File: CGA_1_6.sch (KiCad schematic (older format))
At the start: 19 parts, among them U13 74LS08, U14 74LS32, U28 74LS10, U38 MC6845, U48 74LS51, U49 74LS02, U50 2118, U51 2118, U52 2118, U53 2118, U54 2118, U55 2118, U56 2118, U57 2118, U58 74LS374, U59 74LS374, U60 74LS374, U61 74LS374, U62 74LS125

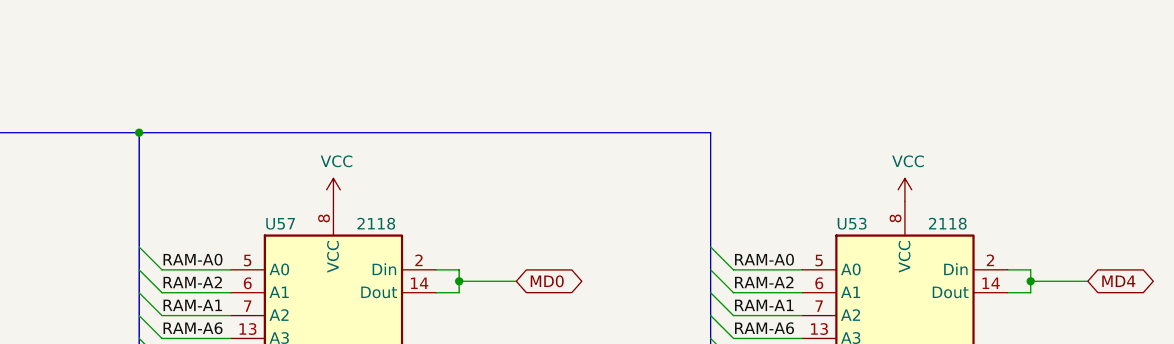
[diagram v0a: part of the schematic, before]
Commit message: Added note on RAM chips
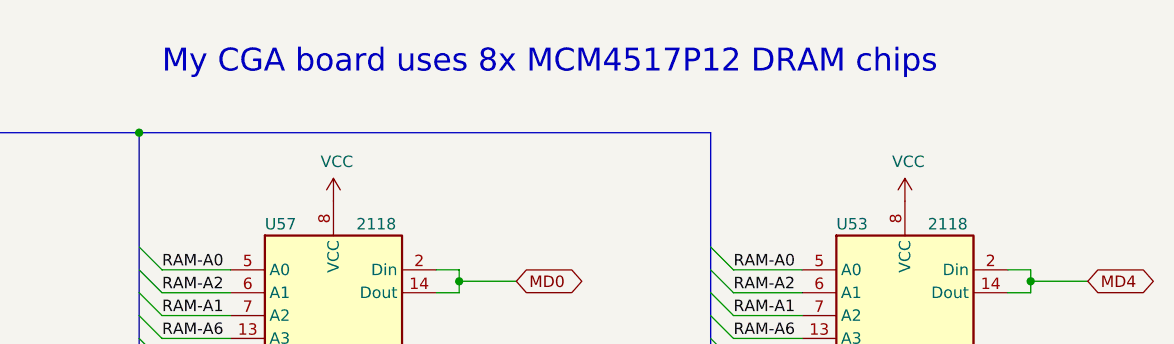
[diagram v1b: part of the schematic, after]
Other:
- note added: "My CGA board uses 8x MCM4517P12 DRAM chips"
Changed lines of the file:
@@
 Wire Bus Line
 	13850 1200 13850 8550
+Text Notes 11450 950  0    100  ~ 0
+My CGA board uses 8x MCM4517P12 DRAM chips
 $EndSCHEMATC

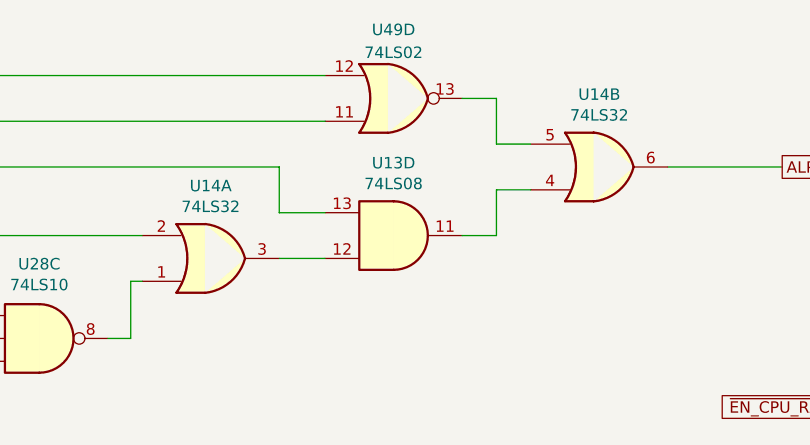
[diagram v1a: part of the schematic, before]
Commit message: Reorganize space between ICs
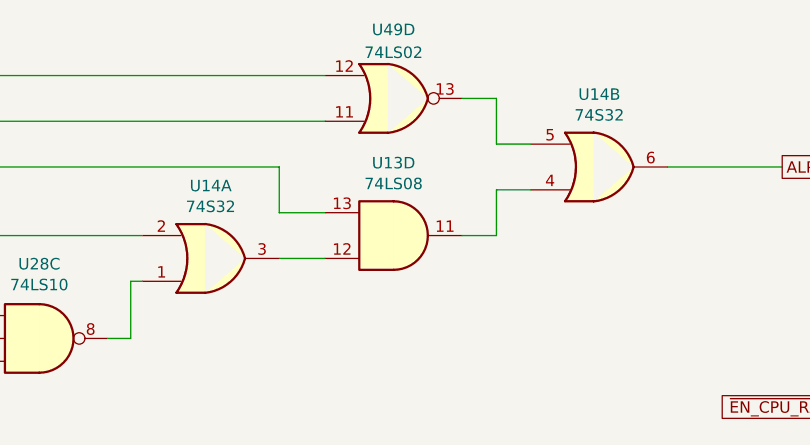
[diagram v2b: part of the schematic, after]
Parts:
- U14: value 74LS32 -> 74S32
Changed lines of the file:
@@
 P 5250 1350
 F 0 "U14" H 5250 1033 50  0000 C CNN
-F 1 "74LS32" H 5250 1124 50  0000 C CNN
+F 1 "74S32" H 5250 1124 50  0000 C CNN
 F 2 "Package_DIP:DIP-14_W7.62mm_LongPads" H 5250 1350 50  0001 C CNN
 F 3 "http://www.ti.com/lit/gpn/sn74LS32" H 5250 1350 50  0001 C CNN
@@
 P 3550 1750
 F 0 "U14" H 3550 1433 50  0000 C CNN
-F 1 "74LS32" H 3550 1524 50  0000 C CNN
+F 1 "74S32" H 3550 1524 50  0000 C CNN
 F 2 "Package_DIP:DIP-14_W7.62mm_LongPads" H 3550 1750 50  0001 C CNN
 F 3 "http://www.ti.com/lit/gpn/sn74LS32" H 3550 1750 50  0001 C CNN

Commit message: Changed footprints, moving components
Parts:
- U13, U14, U28, U48, U62: footprint Package_DIP:DIP-14_W7.62mm_LongPads -> Package_DIP:DIP-14_W7.62mm
- U38: footprint Package_DIP:DIP-40_W15.24mm_LongPads -> Package_DIP:DIP-40_W15.24mm
- U49: footprint (none) -> Package_DIP:DIP-14_W7.62mm
- U50, U51, U52, U53, U54, U55, U56, U57: footprint Package_DIP:DIP-16_W7.62mm_LongPads -> Package_DIP:DIP-16_W7.62mm
- U58, U59, U60, U61: footprint Package_DIP:DIP-20_W7.62mm_LongPads -> Package_DIP:DIP-20_W7.62mm
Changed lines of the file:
@@
 F 0 "U57" H 11900 3800 50  0000 L CNN
 F 1 "2118" H 12300 3800 50  0000 L CNN
-F 2 "Package_DIP:DIP-16_W7.62mm_LongPads" H 12350 2650 50  0001 C CNN
+F 2 "Package_DIP:DIP-16_W7.62mm" H 12350 2650 50  0001 C CNN
 F 3 "" H 12350 2700 50  0001 C CNN
 	1    12350 2700
@@
 F 0 "U56" H 11900 5850 50  0000 L CNN
 F 1 "2118" H 12300 5850 50  0000 L CNN
-F 2 "Package_DIP:DIP-16_W7.62mm_LongPads" H 12350 4700 50  0001 C CNN
+F 2 "Package_DIP:DIP-16_W7.62mm" H 12350 4700 50  0001 C CNN
 F 3 "" H 12350 4750 50  0001 C CNN
 	1    12350 4750
@@
 F 0 "U55" H 11900 7900 50  0000 L CNN
 F 1 "2118" H 12300 7900 50  0000 L CNN
-F 2 "Package_DIP:DIP-16_W7.62mm_LongPads" H 12350 6750 50  0001 C CNN
+F 2 "Package_DIP:DIP-16_W7.62mm" H 12350 6750 50  0001 C CNN
 F 3 "" H 12350 6800 50  0001 C CNN
 	1    12350 6800
@@
 F 0 "U54" H 11900 10050 50  0000 L CNN
 F 1 "2118" H 12300 10050 50  0000 L CNN
-F 2 "Package_DIP:DIP-16_W7.62mm_LongPads" H 12350 8900 50  0001 C CNN
+F 2 "Package_DIP:DIP-16_W7.62mm" H 12350 8900 50  0001 C CNN
 F 3 "" H 12350 8950 50  0001 C CNN
 	1    12350 8950
@@
 F 0 "U53" H 14400 3800 50  0000 L CNN
 F 1 "2118" H 14800 3800 50  0000 L CNN
-F 2 "Package_DIP:DIP-16_W7.62mm_LongPads" H 14850 2650 50  0001 C CNN
+F 2 "Package_DIP:DIP-16_W7.62mm" H 14850 2650 50  0001 C CNN
 F 3 "" H 14850 2700 50  0001 C CNN
 	1    14850 2700
@@
 F 0 "U52" H 14400 5850 50  0000 L CNN
 F 1 "2118" H 14800 5850 50  0000 L CNN
-F 2 "Package_DIP:DIP-16_W7.62mm_LongPads" H 14850 4700 50  0001 C CNN
+F 2 "Package_DIP:DIP-16_W7.62mm" H 14850 4700 50  0001 C CNN
 F 3 "" H 14850 4750 50  0001 C CNN
 	1    14850 4750
@@
 F 0 "U51" H 14400 7900 50  0000 L CNN
 F 1 "2118" H 14800 7900 50  0000 L CNN
-F 2 "Package_DIP:DIP-16_W7.62mm_LongPads" H 14850 6750 50  0001 C CNN
+F 2 "Package_DIP:DIP-16_W7.62mm" H 14850 6750 50  0001 C CNN
 F 3 "" H 14850 6800 50  0001 C CNN
 	1    14850 6800
@@
 F 0 "U50" H 14400 10050 50  0000 L CNN
 F 1 "2118" H 14800 10050 50  0000 L CNN
-F 2 "Package_DIP:DIP-16_W7.62mm_LongPads" H 14850 8900 50  0001 C CNN
+F 2 "Package_DIP:DIP-16_W7.62mm" H 14850 8900 50  0001 C CNN
 F 3 "" H 14850 8950 50  0001 C CNN
 	1    14850 8950
@@
 F 0 "U60" H 8400 2550 50  0000 C CNN
 F 1 "74LS374" H 8850 2550 50  0000 C CNN
-F 2 "Package_DIP:DIP-20_W7.62mm_LongPads" H 8650 1900 50  0001 C CNN
+F 2 "Package_DIP:DIP-20_W7.62mm" H 8650 1900 50  0001 C CNN
 F 3 "http://www.ti.com/lit/gpn/sn74LS374" H 8650 1900 50  0001 C CNN
 	1    8650 1900
@@
 F 0 "U61" H 8400 4650 50  0000 C CNN
 F 1 "74LS374" H 8850 4650 50  0000 C CNN
-F 2 "Package_DIP:DIP-20_W7.62mm_LongPads" H 8650 4000 50  0001 C CNN
+F 2 "Package_DIP:DIP-20_W7.62mm" H 8650 4000 50  0001 C CNN
 F 3 "http://www.ti.com/lit/gpn/sn74LS374" H 8650 4000 50  0001 C CNN
 	1    8650 4000
@@
 F 0 "U59" H 8400 6750 50  0000 C CNN
 F 1 "74LS374" H 8850 6750 50  0000 C CNN
-F 2 "Package_DIP:DIP-20_W7.62mm_LongPads" H 8650 6100 50  0001 C CNN
+F 2 "Package_DIP:DIP-20_W7.62mm" H 8650 6100 50  0001 C CNN
 F 3 "http://www.ti.com/lit/gpn/sn74LS374" H 8650 6100 50  0001 C CNN
 	1    8650 6100
@@
 F 0 "U58" H 8400 8850 50  0000 C CNN
 F 1 "74LS374" H 8850 8850 50  0000 C CNN
-F 2 "Package_DIP:DIP-20_W7.62mm_LongPads" H 8650 8200 50  0001 C CNN
+F 2 "Package_DIP:DIP-20_W7.62mm" H 8650 8200 50  0001 C CNN
 F 3 "http://www.ti.com/lit/gpn/sn74LS374" H 8650 8200 50  0001 C CNN
 	1    8650 8200
@@
 F 0 "U62" H 8000 9917 50  0000 C CNN
 F 1 "74LS125" H 8000 9826 50  0000 C CNN
-F 2 "Package_DIP:DIP-14_W7.62mm_LongPads" H 8000 9600 50  0001 C CNN
+F 2 "Package_DIP:DIP-14_W7.62mm" H 8000 9600 50  0001 C CNN
 F 3 "http://www.ti.com/lit/gpn/sn74LS125" H 8000 9600 50  0001 C CNN
 	1    8000 9600
@@
 F 0 "U49" H 6900 10875 50  0000 C CNN
 F 1 "74LS02" H 6900 10784 50  0000 C CNN
-F 2 "" H 6900 10550 50  0001 C CNN
+F 2 "Package_DIP:DIP-14_W7.62mm" H 6900 10550 50  0001 C CNN
 F 3 "http://www.ti.com/lit/gpn/sn74ls02" H 6900 10550 50  0001 C CNN
 	3    6900 10550
@@
 F 0 "U48" H 5950 11075 50  0000 C CNN
 F 1 "74LS51" H 5950 10984 50  0000 C CNN
-F 2 "Package_DIP:DIP-14_W7.62mm_LongPads" H 5950 10550 50  0001 C CNN
+F 2 "Package_DIP:DIP-14_W7.62mm" H 5950 10550 50  0001 C CNN
 F 3 "http://www.ti.com/lit/ds/symlink/sn74ls51.pdf" H 5950 10550 50  0001 C CNN
 	1    5950 10550
@@
 F 0 "U38" H 2850 8550 50  0000 C CNN
 F 1 "MC6845" H 3650 8550 50  0000 C CNN
-F 2 "Package_DIP:DIP-40_W15.24mm_LongPads" H 3350 5850 50  0001 L CNN
+F 2 "Package_DIP:DIP-40_W15.24mm" H 3350 5850 50  0001 L CNN
 F 3 "http://pdf.datasheetcatalog.com/datasheet_pdf/motorola/MC6845L_and_MC6845P.pdf" H 3300 7200 50  0001 C CNN
 	1    3300 7200
@@
 F 0 "U49" H 4350 750 50  0000 C CNN
 F 1 "74LS02" H 4350 850 50  0000 C CNN
-F 2 "" H 4350 1050 50  0001 C CNN
+F 2 "Package_DIP:DIP-14_W7.62mm" H 4350 1050 50  0001 C CNN
 F 3 "http://www.ti.com/lit/gpn/sn74ls02" H 4350 1050 50  0001 C CNN
 	4    4350 1050
@@
 F 0 "U14" H 5250 1033 50  0000 C CNN
 F 1 "74S32" H 5250 1124 50  0000 C CNN
-F 2 "Package_DIP:DIP-14_W7.62mm_LongPads" H 5250 1350 50  0001 C CNN
+F 2 "Package_DIP:DIP-14_W7.62mm" H 5250 1350 50  0001 C CNN
 F 3 "http://www.ti.com/lit/gpn/sn74LS32" H 5250 1350 50  0001 C CNN
 	2    5250 1350
@@
 F 0 "U13" H 4350 1333 50  0000 C CNN
 F 1 "74LS08" H 4350 1424 50  0000 C CNN
-F 2 "Package_DIP:DIP-14_W7.62mm_LongPads" H 4350 1650 50  0001 C CNN
+F 2 "Package_DIP:DIP-14_W7.62mm" H 4350 1650 50  0001 C CNN
 F 3 "http://www.ti.com/lit/gpn/sn74LS08" H 4350 1650 50  0001 C CNN
 	4    4350 1650
@@
 F 0 "U14" H 3550 1433 50  0000 C CNN
 F 1 "74S32" H 3550 1524 50  0000 C CNN
-F 2 "Package_DIP:DIP-14_W7.62mm_LongPads" H 3550 1750 50  0001 C CNN
+F 2 "Package_DIP:DIP-14_W7.62mm" H 3550 1750 50  0001 C CNN
 F 3 "http://www.ti.com/lit/gpn/sn74LS32" H 3550 1750 50  0001 C CNN
 	1    3550 1750
@@
 F 0 "U28" H 2800 2425 50  0000 C CNN
 F 1 "74LS10" H 2800 2334 50  0000 C CNN
-F 2 "Package_DIP:DIP-14_W7.62mm_LongPads" H 2800 2100 50  0001 C CNN
+F 2 "Package_DIP:DIP-14_W7.62mm" H 2800 2100 50  0001 C CNN
 F 3 "http://www.ti.com/lit/gpn/sn74LS10" H 2800 2100 50  0001 C CNN
 	3    2800 2100
@@
 Wire Wire Line
 	11450 6200 11750 6200
+Text Notes 11450 950  0    100  ~ 0
+My CGA board uses 8x MCM4517P12 DRAM chips
 Wire Bus Line
 	9650 1200 9650 8550
@@
 Wire Bus Line
 	13850 1200 13850 8550
-Text Notes 11450 950  0    100  ~ 0
-My CGA board uses 8x MCM4517P12 DRAM chips
 $EndSCHEMATC

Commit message: connect the two NC in DRAM to GND, so ideally 4164 and 41256 can be used
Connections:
- net GND: now also U50.1 (NC), U50.9 (NC), U51.1 (NC), U51.9 (NC), U52.1 (NC), U52.9 (NC), U53.1 (NC), U53.9 (NC), U54.1 (NC), U54.9 (NC), U55.1 (NC), U55.9 (NC), U56.1 (NC), U56.9 (NC), U57.1 (NC), U57.9 (NC)
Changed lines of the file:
@@
 Text Notes 11450 950  0    100  ~ 0
 My CGA board uses 8x MCM4517P12 DRAM chips
+Wire Wire Line
+	12650 2300 12750 2300
+Wire Wire Line
+	12750 2300 12750 2350
+Wire Wire Line
+	12750 2400 12650 2400
+$Comp
+L power:GND #PWR?
+U 1 1 6084F132
+P 12850 2500
+F 0 "#PWR?" H 12850 2250 50  0001 C CNN
+F 1 "GND" H 12855 2327 50  0000 C CNN
+F 2 "" H 12850 2500 50  0001 C CNN
+F 3 "" H 12850 2500 50  0001 C CNN
+	1    12850 2500
+	1    0    0    -1
+$EndComp
+Wire Wire Line
+	12750 2350 12850 2350
+Wire Wire Line
+	12850 2350 12850 2500
+Connection ~ 12750 2350
+Wire Wire Line
+	12750 2350 12750 2400
+Wire Wire Line
+	15150 2300 15250 2300
+Wire Wire Line
+	15250 2300 15250 2350
+Wire Wire Line
+	15250 2400 15150 2400
+$Comp
+L power:GND #PWR?
+U 1 1 6087581A
+P 15350 2500
+F 0 "#PWR?" H 15350 2250 50  0001 C CNN
+F 1 "GND" H 15355 2327 50  0000 C CNN
+F 2 "" H 15350 2500 50  0001 C CNN
+F 3 "" H 15350 2500 50  0001 C CNN
+	1    15350 2500
+	1    0    0    -1
+$EndComp
+Wire Wire Line
+	15250 2350 15350 2350
+Wire Wire Line
+	15350 2350 15350 2500
+Connection ~ 15250 2350
+Wire Wire Line
+	15250 2350 15250 2400
+Wire Wire Line
+	12650 4350 12750 4350
+Wire Wire Line
+	12750 4350 12750 4400
+Wire Wire Line
+	12750 4450 12650 4450
+$Comp
+L power:GND #PWR?
+U 1 1 6089A5C0
+P 12850 4550
+F 0 "#PWR?" H 12850 4300 50  0001 C CNN
+F 1 "GND" H 12855 4377 50  0000 C CNN
+F 2 "" H 12850 4550 50  0001 C CNN
+F 3 "" H 12850 4550 50  0001 C CNN
+	1    12850 4550
+	1    0    0    -1
+$EndComp
+Wire Wire Line
+	12750 4400 12850 4400
+Wire Wire Line
+	12850 4400 12850 4550
+Connection ~ 12750 4400
+Wire Wire Line
+	12750 4400 12750 4450
+Wire Wire Line
+	15150 4350 15250 4350
+Wire Wire Line
+	15250 4350 15250 4400
+Wire Wire Line
+	15250 4450 15150 4450
+$Comp
+L power:GND #PWR?
+U 1 1 608BFDC6
+P 15350 4550
+F 0 "#PWR?" H 15350 4300 50  0001 C CNN
+F 1 "GND" H 15355 4377 50  0000 C CNN
+F 2 "" H 15350 4550 50  0001 C CNN
+F 3 "" H 15350 4550 50  0001 C CNN
+	1    15350 4550
+	1    0    0    -1
+$EndComp
+Wire Wire Line
+	15250 4400 15350 4400
+Wire Wire Line
+	15350 4400 15350 4550
+Connection ~ 15250 4400
+Wire Wire Line
+	15250 4400 15250 4450
+Wire Wire Line
+	12650 6400 12750 6400
+Wire Wire Line
+	12750 6400 12750 6450
+Wire Wire Line
+	12750 6500 12650 6500
+$Comp
+L power:GND #PWR?
+U 1 1 608E60A7
+P 12850 6600
+F 0 "#PWR?" H 12850 6350 50  0001 C CNN
+F 1 "GND" H 12855 6427 50  0000 C CNN
+F 2 "" H 12850 6600 50  0001 C CNN
+F 3 "" H 12850 6600 50  0001 C CNN
+	1    12850 6600
+	1    0    0    -1
+$EndComp
+Wire Wire Line
+	12750 6450 12850 6450
+Wire Wire Line
+	12850 6450 12850 6600
+Connection ~ 12750 6450
+Wire Wire Line
+	12750 6450 12750 6500
+Wire Wire Line
+	15150 6400 15250 6400
+Wire Wire Line
+	15250 6400 15250 6450
+Wire Wire Line
+	15250 6500 15150 6500
+$Comp
+L power:GND #PWR?
+U 1 1 6090D358
+P 15350 6600
+F 0 "#PWR?" H 15350 6350 50  0001 C CNN
+F 1 "GND" H 15355 6427 50  0000 C CNN
+F 2 "" H 15350 6600 50  0001 C CNN
+F 3 "" H 15350 6600 50  0001 C CNN
+	1    15350 6600
+	1    0    0    -1
+$EndComp
+Wire Wire Line
+	15250 6450 15350 6450
+Wire Wire Line
+	15350 6450 15350 6600
+Connection ~ 15250 6450
+Wire Wire Line
+	15250 6450 15250 6500
+Wire Wire Line
+	12650 8550 12750 8550
+Wire Wire Line
+	12750 8550 12750 8600
+Wire Wire Line
+	12750 8650 12650 8650
+$Comp
+L power:GND #PWR?
+U 1 1 6093520C
+P 12850 8750
+F 0 "#PWR?" H 12850 8500 50  0001 C CNN
+F 1 "GND" H 12855 8577 50  0000 C CNN
+F 2 "" H 12850 8750 50  0001 C CNN
+F 3 "" H 12850 8750 50  0001 C CNN
+	1    12850 8750
+	1    0    0    -1
+$EndComp
+Wire Wire Line
+	12750 8600 12850 8600
+Wire Wire Line
+	12850 8600 12850 8750
+Connection ~ 12750 8600
+Wire Wire Line
+	12750 8600 12750 8650
+Wire Wire Line
+	15150 8550 15250 8550
+Wire Wire Line
+	15250 8550 15250 8600
+Wire Wire Line
+	15250 8650 15150 8650
+$Comp
+L power:GND #PWR?
+U 1 1 6095DEA2
+P 15350 8750
+F 0 "#PWR?" H 15350 8500 50  0001 C CNN
+F 1 "GND" H 15355 8577 50  0000 C CNN
+F 2 "" H 15350 8750 50  0001 C CNN
+F 3 "" H 15350 8750 50  0001 C CNN
+	1    15350 8750
+	1    0    0    -1
+$EndComp
+Wire Wire Line
+	15250 8600 15350 8600
+Wire Wire Line
+	15350 8600 15350 8750
+Connection ~ 15250 8600
+Wire Wire Line
+	15250 8600 15250 8650
 Wire Bus Line
 	9650 1200 9650 8550

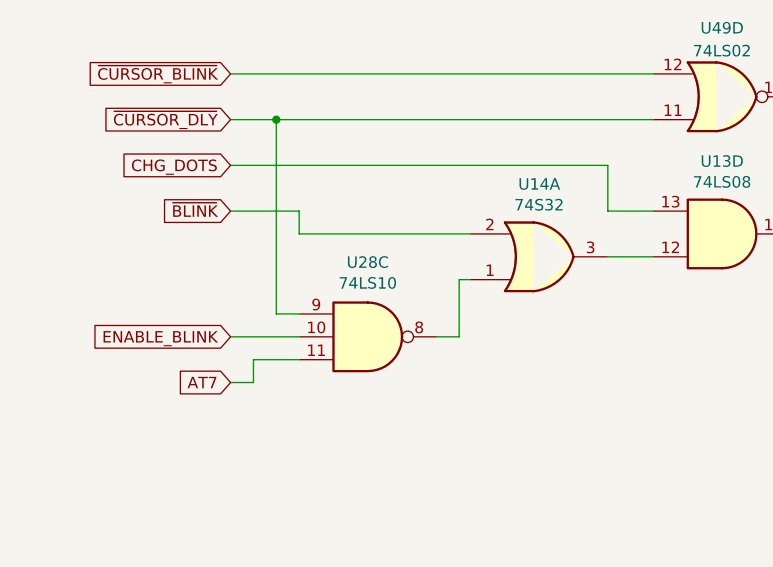
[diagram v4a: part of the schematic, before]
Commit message: Replaced 74LS10 for U28 with 74S10
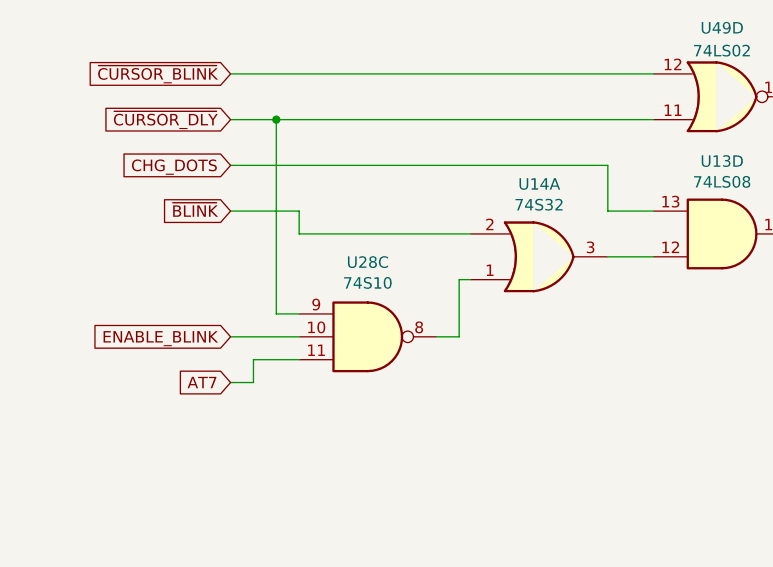
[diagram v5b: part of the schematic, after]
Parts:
- U28: value 74LS10 -> 74S10
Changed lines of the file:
@@
 P 2800 2100
 F 0 "U28" H 2800 2425 50  0000 C CNN
-F 1 "74LS10" H 2800 2334 50  0000 C CNN
+F 1 "74S10" H 2800 2334 50  0000 C CNN
 F 2 "Package_DIP:DIP-14_W7.62mm" H 2800 2100 50  0001 C CNN
 F 3 "http://www.ti.com/lit/gpn/sn74LS10" H 2800 2100 50  0001 C CNN
@@
 	12750 2400 12650 2400
 $Comp
-L power:GND #PWR?
+L power:GND #PWR0241
 U 1 1 6084F132
 P 12850 2500
-F 0 "#PWR?" H 12850 2250 50  0001 C CNN
+F 0 "#PWR0241" H 12850 2250 50  0001 C CNN
 F 1 "GND" H 12855 2327 50  0000 C CNN
 F 2 "" H 12850 2500 50  0001 C CNN
@@
 	15250 2400 15150 2400
 $Comp
-L power:GND #PWR?
+L power:GND #PWR0242
 U 1 1 6087581A
 P 15350 2500
-F 0 "#PWR?" H 15350 2250 50  0001 C CNN
+F 0 "#PWR0242" H 15350 2250 50  0001 C CNN
 F 1 "GND" H 15355 2327 50  0000 C CNN
 F 2 "" H 15350 2500 50  0001 C CNN
@@
 	12750 4450 12650 4450
 $Comp
-L power:GND #PWR?
+L power:GND #PWR0243
 U 1 1 6089A5C0
 P 12850 4550
-F 0 "#PWR?" H 12850 4300 50  0001 C CNN
+F 0 "#PWR0243" H 12850 4300 50  0001 C CNN
 F 1 "GND" H 12855 4377 50  0000 C CNN
 F 2 "" H 12850 4550 50  0001 C CNN
@@
 	15250 4450 15150 4450
 $Comp
-L power:GND #PWR?
+L power:GND #PWR0244
 U 1 1 608BFDC6
 P 15350 4550
-F 0 "#PWR?" H 15350 4300 50  0001 C CNN
+F 0 "#PWR0244" H 15350 4300 50  0001 C CNN
 F 1 "GND" H 15355 4377 50  0000 C CNN
 F 2 "" H 15350 4550 50  0001 C CNN
@@
 	12750 6500 12650 6500
 $Comp
-L power:GND #PWR?
+L power:GND #PWR0245
 U 1 1 608E60A7
 P 12850 6600
-F 0 "#PWR?" H 12850 6350 50  0001 C CNN
+F 0 "#PWR0245" H 12850 6350 50  0001 C CNN
 F 1 "GND" H 12855 6427 50  0000 C CNN
 F 2 "" H 12850 6600 50  0001 C CNN
@@
 	15250 6500 15150 6500
 $Comp
-L power:GND #PWR?
+L power:GND #PWR0246
 U 1 1 6090D358
 P 15350 6600
-F 0 "#PWR?" H 15350 6350 50  0001 C CNN
+F 0 "#PWR0246" H 15350 6350 50  0001 C CNN
 F 1 "GND" H 15355 6427 50  0000 C CNN
 F 2 "" H 15350 6600 50  0001 C CNN
@@
 	12750 8650 12650 8650
 $Comp
-L power:GND #PWR?
+L power:GND #PWR0247
 U 1 1 6093520C
 P 12850 8750
-F 0 "#PWR?" H 12850 8500 50  0001 C CNN
+F 0 "#PWR0247" H 12850 8500 50  0001 C CNN
 F 1 "GND" H 12855 8577 50  0000 C CNN
 F 2 "" H 12850 8750 50  0001 C CNN
@@
 	15250 8650 15150 8650
 $Comp
-L power:GND #PWR?
+L power:GND #PWR0248
 U 1 1 6095DEA2
 P 15350 8750
-F 0 "#PWR?" H 15350 8500 50  0001 C CNN
+F 0 "#PWR0248" H 15350 8500 50  0001 C CNN
 F 1 "GND" H 15355 8577 50  0000 C CNN
 F 2 "" H 15350 8750 50  0001 C CNN
